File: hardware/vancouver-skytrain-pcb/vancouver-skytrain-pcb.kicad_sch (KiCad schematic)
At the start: 407 parts, among them J1 Conn_01x04, J2 Conn_01x02, J2_POWER_IN1 Conn_01x02, J3 Conn_01x02, J3_PROGRAMING_PIN1 Conn_01x06, J4 Conn_01x09, Q1 PN2222A, Q2 PN2222A, U1 74AHC1G125

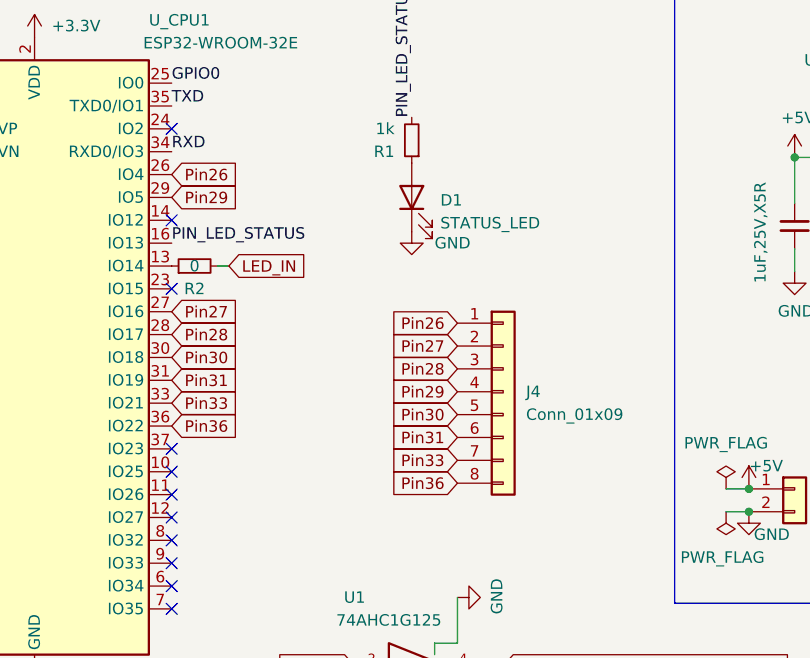
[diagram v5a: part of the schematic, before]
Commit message: Updating the parts that are DNP
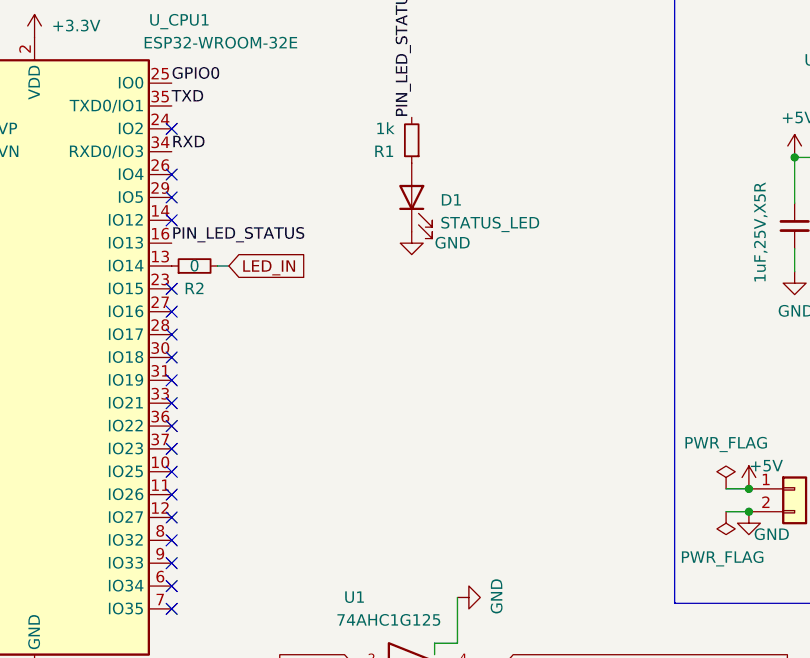
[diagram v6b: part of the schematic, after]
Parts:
- removed J4: Conn_01x09, Connector_PinHeader_2.54mm:PinHeader_1x08_P2.54mm_Vertical, symbol Connector_Generic:Conn_01x08
- H1, H2, H3, H4, J1, J2, J2_POWER_IN1, J3, J3_PROGRAMING_PIN1, TP1, TP10, TP100, TP101, TP102, TP103, TP104, TP105, TP106, TP107, TP108, TP109, TP11, TP110, TP111, TP112, TP113, TP114, TP115, TP116, TP117, TP118, TP119, TP12, TP120, TP121, TP122, TP123, TP124, TP125, TP126, TP13, TP14, TP15, TP16, TP17, TP18, TP19, TP2, TP20, TP21, TP22, TP23, TP24, TP25, TP26, TP27, TP28, TP29, TP3, TP30, TP31, TP32, TP33, TP34, TP35, TP36, TP37, TP38, TP39, TP4, TP40, TP41, TP42, TP43, TP44, TP45, TP46, TP47, TP48, TP49, TP5, TP50, TP51, TP52, TP53, TP54, TP55, TP56, TP57, TP58, TP59, TP6, TP60, TP61, TP62, TP63, TP64, TP65, TP66, TP67, TP68, TP69, TP7, TP70, TP71, TP72, TP73, TP74, TP75, TP76, TP77, TP78, TP79, TP8, TP80, TP81, TP82, TP83, TP84, TP85, TP86, TP87, TP88, TP89, TP9, TP90, TP91, TP92, TP93, TP94, TP95, TP96, TP97, TP98, TP99: LCSC (none) -> DNP
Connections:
- net Pin26: no longer names the net of U_CPU1.26 (IO4)
- net Pin27: no longer names the net of U_CPU1.27 (IO16)
- net Pin28: no longer names the net of U_CPU1.28 (IO17)
- net Pin29: no longer names the net of U_CPU1.29 (IO5)
- net Pin30: no longer names the net of U_CPU1.30 (IO18)
- net Pin31: no longer names the net of U_CPU1.31 (IO19)
- net Pin33: no longer names the net of U_CPU1.33 (IO21)
- net Pin36: no longer names the net of U_CPU1.36 (IO22)
- no-connect marks 14 -> 22
